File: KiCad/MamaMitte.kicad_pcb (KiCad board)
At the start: 2 copper layers, 61.8 x 37 mm, 29 parts, among them J1 WSCART, Q1 2SC4097, U1 BANDAI2003, U2 S3511A, U3 MBM29LV800TA, U4 TC7W04FK, U5 TFMM53xx, X1 SPT2AF-6PF20PPM

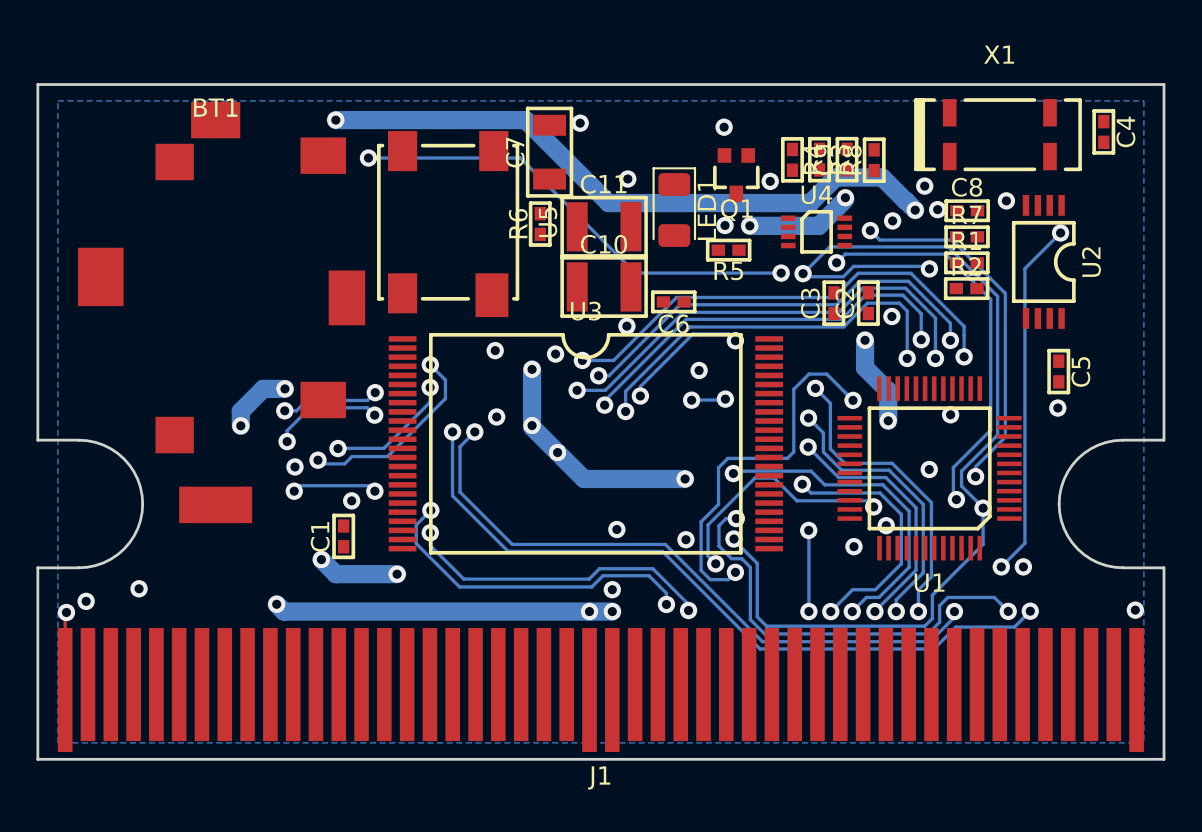
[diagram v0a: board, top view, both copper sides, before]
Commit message: Begin routing top
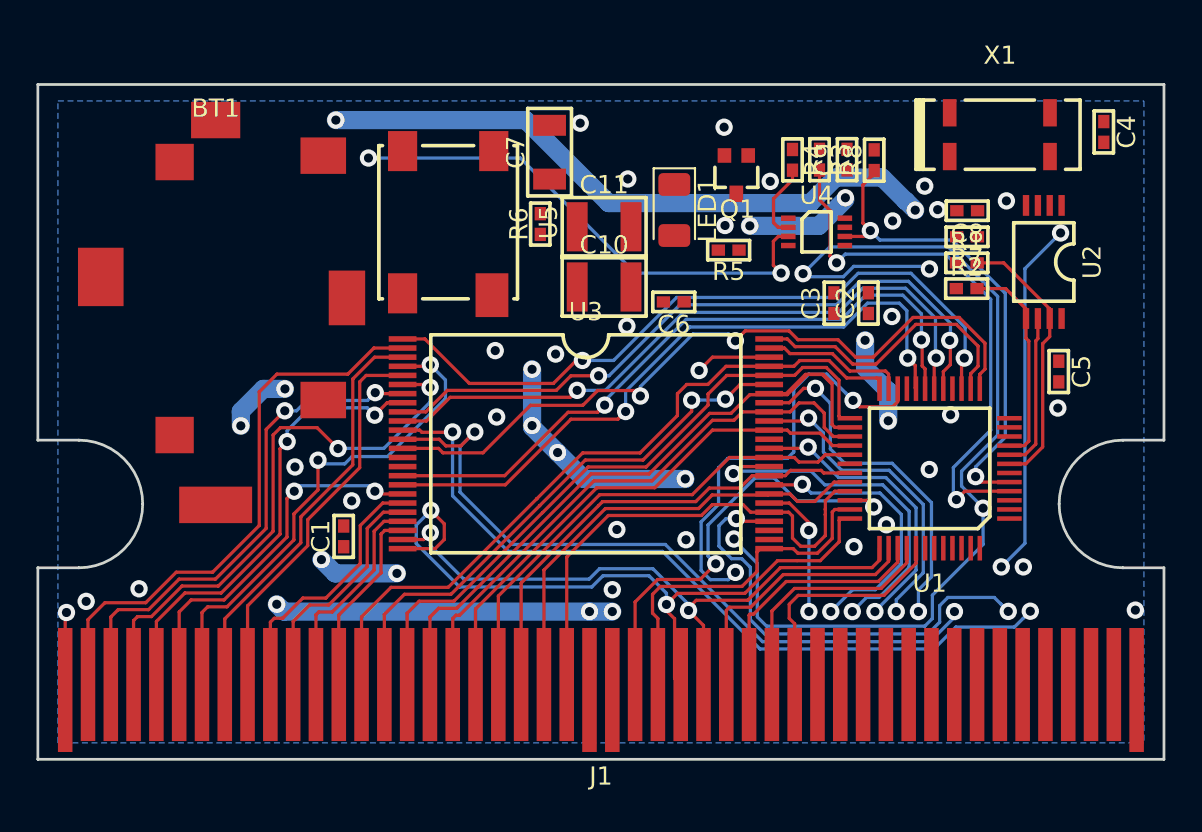
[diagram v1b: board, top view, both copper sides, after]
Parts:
- turned C8 to 180 degrees
- turned R7 to 180 degrees
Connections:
- net /Memory/A21 renamed /Memory/SA21
- BT1 pad 1: Net-(BT1-Pad1) -> /Real-Time Clock/VBAT
- C5 pad 1: /Real-Time Clock/VBAT -> /Real-Time Clock/VRTC
- C8 pad 1: /Real-Time Clock/VBAT -> /Real-Time Clock/VRTC
- J1 pad 0: GND -> (no net)
- R7 pad 1: /Real-Time Clock/VBAT -> /Real-Time Clock/VRTC
- R7 pad 2: Net-(BT1-Pad1) -> /Real-Time Clock/VBAT
- U1 pad 14: A16 -> /Memory/SA16
- U1 pad 15: A15 -> /Memory/SA15
- U1 pad 17: /Memory/A20 -> /Memory/SA19
- U1 pad 18: /Memory/A19 -> /Memory/SA20
- U1 pad 19: A18 -> /Memory/SA18
- U1 pad 20: A17 -> /Memory/SA17
- U2 pad 8: /Real-Time Clock/VBAT -> /Real-Time Clock/VRTC
- U3 pad 1: A15 -> /Memory/SA15
- U3 pad 10: /Memory/A20 -> /Memory/SA20
- U3 pad 16: A18 -> /Memory/SA18
- U3 pad 17: A17 -> /Memory/SA17
- U3 pad 48: A16 -> /Memory/SA16
- U3 pad 9: /Memory/A19 -> /Memory/SA19
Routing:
- net Q15: track 0.00 -> 39.5 mm
- net /Memory/SA15: track 0.00 -> 39.0 mm, vias 0 -> 2
- net Q6: track 0.00 -> 38.8 mm
- net /Memory/SA19: track 0.00 -> 37.7 mm, vias 0 -> 2
- net /Memory/SA18: track 0.00 -> 37.3 mm, vias 0 -> 2
- net /Memory/SA17: track 0.00 -> 37.1 mm, vias 0 -> 2
- net /Memory/SA20: track 0.00 -> 36.9 mm, vias 0 -> 2
- net Q7: track 0.00 -> 36.4 mm
- net /Memory/SA21: track 7.08 -> 40.4 mm
- net Q5: track 0.00 -> 31.5 mm
- net A10: track 0.00 -> 31.2 mm, vias 0 -> 2
- net Q14: track 0.00 -> 30.5 mm, vias 0 -> 2
- net Q4: track 0.00 -> 29.1 mm
- net Q0: track 0.00 -> 27.7 mm
- net Q3: track 0.00 -> 27.5 mm
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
